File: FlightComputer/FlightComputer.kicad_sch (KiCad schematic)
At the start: 0 parts

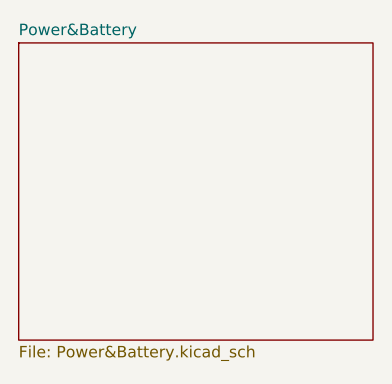
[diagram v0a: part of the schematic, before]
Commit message: Adding 3.3V regulator, usb c connector, battery connector and calculations sheet
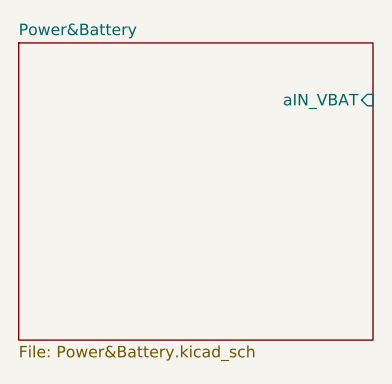
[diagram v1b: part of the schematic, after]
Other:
- sheet Power&Battery ports: added aIN_VBAT; removed none
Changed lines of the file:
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@@
+			)
+		)
+		(pin "aIN_VBAT" input
+			(at 74.93 39.37 0)
+			(effects
+				(font
+					(size 1.27 1.27)
+				)
+				(justify right)
 			)
 		)

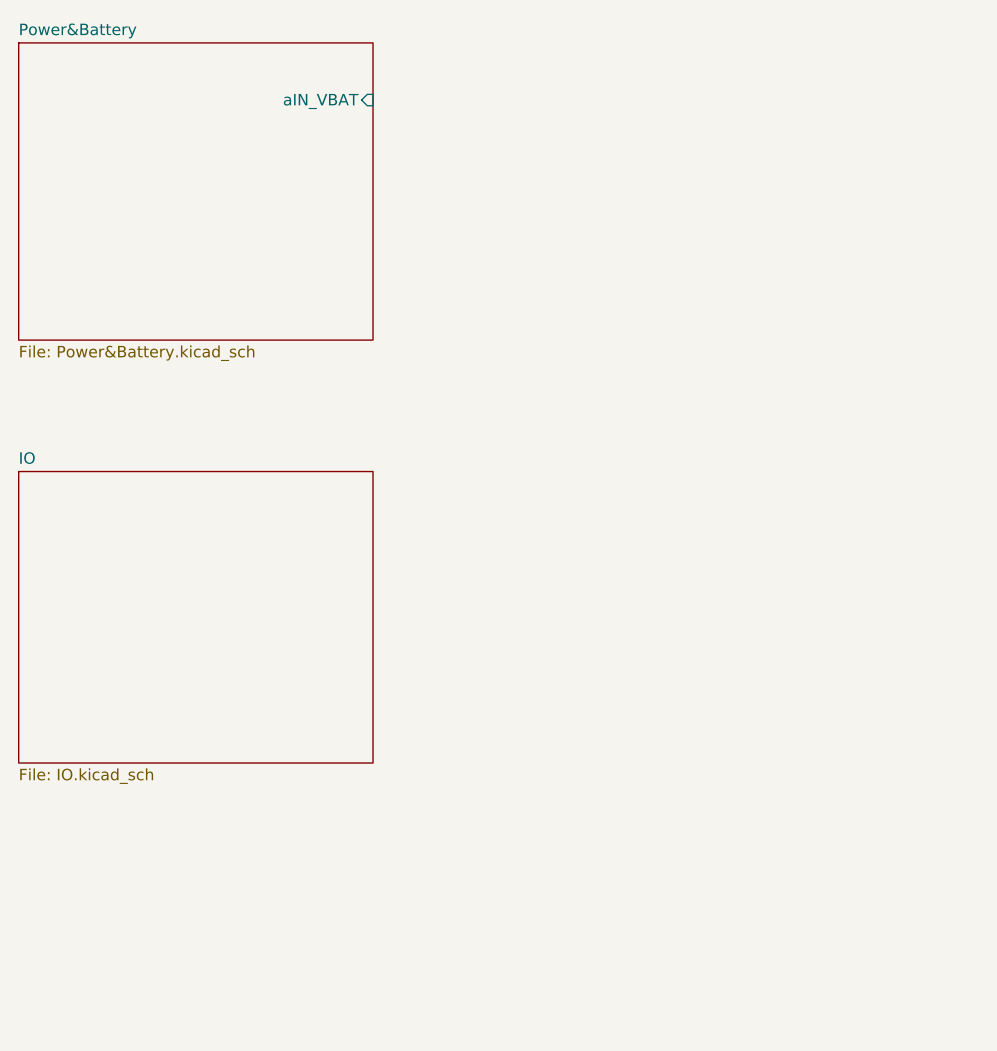
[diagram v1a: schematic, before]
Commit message: Updating calculations, sensors page and adding micro page
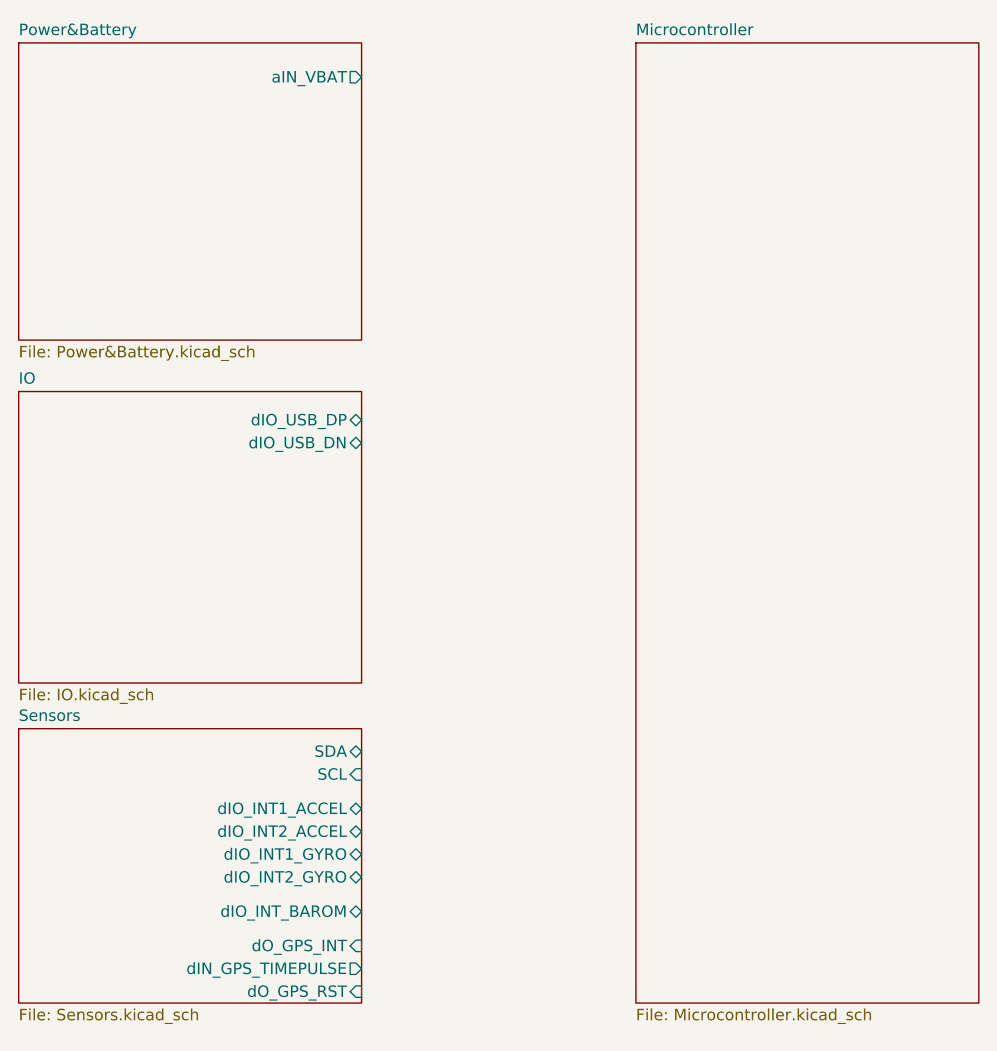
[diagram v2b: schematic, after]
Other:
- added sheet Microcontroller (Microcontroller.kicad_sch)
- added sheet Sensors (Sensors.kicad_sch)
- sheet IO ports: added dIO_USB_DN, dIO_USB_DP; removed none
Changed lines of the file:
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@@
 	(paper "A4")
 	(sheet
-		(at 35.56 80.645)
-		(size 39.37 32.385)
+		(at 35.56 109.22)
+		(size 38.1 30.48)
+		(exclude_from_sim no)
+		(in_bom yes)
+		(on_board yes)
+		(dnp no)
+		(fields_autoplaced yes)
+		(stroke
+			(width 0.1524)
+			(type solid)
+		)
+		(fill
+			(color 0 0 0 0.0000)
+		)
+		(property "Sheetname" "Sensors"
+			(at 35.56 108.5084 0)
+			(effects
+				(font
+					(size 1.27 1.27)
+				)
+				(justify left bottom)
+			)
+		)
+		(property "Sheetfile" "Sensors.kicad_sch"
+			(at 35.56 140.2846 0)
+			(effects
+				(font
+					(size 1.27 1.27)
+				)
+				(justify left top)
+			)
+		)
+		(pin "dIO_INT1_ACCEL" bidirectional
+			(at 73.66 118.11 0)
+			(effects
+				(font
+					(size 1.27 1.27)
+				)
+				(justify right)
+			)
+		)
+		(pin "dIO_INT2_GYRO" bidirectional
+			(at 73.66 125.73 0)
+			(effects
+				(font
+					(size 1.27 1.27)
+				)
+				(justify right)
+			)
+		)
+		(pin "dIN_GPS_TIMEPULSE" output
+			(at 73.66 135.89 0)
+			(effects
+				(font
+					(size 1.27 1.27)
+				)
+				(justify right)
+			)
+		)
+		(pin "dO_GPS_INT" input
+			(at 73.66 133.35 0)
+			(effects
+				(font
+					(size 1.27 1.27)
+				)
+				(justify right)
+			)
+		)
+		(pin "dO_GPS_RST" input
+			(at 73.66 138.43 0)
+			(effects
+				(font
+					(size 1.27 1.27)
+				)
+				(justify right)
+			)
+		)
+		(pin "SDA" bidirectional
+			(at 73.66 111.76 0)
+			(effects
+				(font
+					(size 1.27 1.27)
+				)
+				(justify right)
+			)
+		)
+		(pin "SCL" input
+			(at 73.66 114.3 0)
+			(effects
+				(font
+					(size 1.27 1.27)
+				)
+				(justify right)
+			)
+		)
+		(pin "dIO_INT2_ACCEL" bidirectional
+			(at 73.66 120.65 0)
+			(effects
+				(font
+					(size 1.27 1.27)
+				)
+				(justify right)
+			)
+		)
+		(pin "dIO_INT1_GYRO" bidirectional
+			(at 73.66 123.19 0)
+			(effects
+				(font
+					(size 1.27 1.27)
+				)
+				(justify right)
+			)
+		)
+		(pin "dIO_INT_BAROM" bidirectional
+			(at 73.66 129.54 0)
+			(effects
+				(font
+					(size 1.27 1.27)
+				)
+				(justify right)
+			)
+		)
+		(instances
+			(project "FlightComputer"
+				(path "/e49ed6f8-44fe-4a80-bc0f-4dd2a2b50b4e"
+					(page "4")
+				)
+			)
+		)
+	)
+	(sheet
+		(at 35.56 71.755)
+		(size 38.1 32.385)
 		(exclude_from_sim no)
 		(in_bom yes)
@@
 		)
 		(property "Sheetname" "IO"
-			(at 35.56 79.9334 0)
+			(at 35.56 71.0434 0)
 			(effects
 				(font
@@
 		)
 		(property "Sheetfile" "IO.kicad_sch"
-			(at 35.56 113.6146 0)
-			(effects
-				(font
-					(size 1.27 1.27)
-				)
-				(justify left top)
+			(at 35.56 104.7246 0)
+			(effects
+				(font
+					(size 1.27 1.27)
+				)
+				(justify left top)
+			)
+		)
+		(pin "dIO_USB_DP" bidirectional
+			(at 73.66 74.93 0)
+			(effects
+				(font
+					(size 1.27 1.27)
+				)
+				(justify right)
+			)
+		)
+		(pin "dIO_USB_DN" bidirectional
+			(at 73.66 77.47 0)
+			(effects
+				(font
+					(size 1.27 1.27)
+				)
+				(justify right)
 			)
 		)
@@
 	)
 	(sheet
+		(at 104.14 33.02)
+		(size 38.1 106.68)
+		(exclude_from_sim no)
+		(in_bom yes)
+		(on_board yes)
+		(dnp no)
+		(fields_autoplaced yes)
+		(stroke
+			(width 0.1524)
+			(type solid)
+		)
+		(fill
+			(color 0 0 0 0.0000)
+		)
+		(property "Sheetname" "Microcontroller"
+			(at 104.14 32.3084 0)
+			(effects
+				(font
+					(size 1.27 1.27)
+				)
+				(justify left bottom)
+			)
+		)
+		(property "Sheetfile" "Microcontroller.kicad_sch"
+			(at 104.14 140.2846 0)
+			(effects
+				(font
+					(size 1.27 1.27)
+				)
+				(justify left top)
+			)
+		)
+		(instances
+			(project "FlightComputer"
+				(path "/e49ed6f8-44fe-4a80-bc0f-4dd2a2b50b4e"
+					(page "5")
+				)
+			)
+		)
+	)
+	(sheet
 		(at 35.56 33.02)
-		(size 39.37 33.02)
+		(size 38.1 33.02)
 		(exclude_from_sim no)
 		(in_bom yes)
@@
 			)
 		)
-		(pin "aIN_VBAT" input
-			(at 74.93 39.37 0)
-			(effects
-				(font
+		(pin "aIN_VBAT" output
+			(at 73.66 36.83 0)
+			(effects
+				(font

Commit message: Various updates
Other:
- sheet IO ports: added JTAG_NRST, JTAG_TCK, JTAG_TDI, JTAG_TDO, JTAG_TMS; removed none
- sheet Microcontroller ports: added JTAG_NRST, JTAG_TCK, JTAG_TDI, JTAG_TDO, JTAG_TMS, SCL, SDA, dIO_INT1_ACCEL, dIO_INT1_GYRO, dIO_INT2_ACCEL, dIO_INT2_GYRO, dIO_USB_DN, dIO_USB_DP; removed none
- company: (none) -> MD
